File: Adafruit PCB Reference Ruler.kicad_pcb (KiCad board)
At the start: 2 copper layers, 101 x 25.4 mm, 63 parts

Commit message: Starting on schematic to PCB design
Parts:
- removed E$16, E$60, E$63: , Adafruit PCB Reference Ruler:0201
- removed E$23, E$61: , Adafruit PCB Reference Ruler:0402
- removed E$24, E$62: , Adafruit PCB Reference Ruler:0603
- removed E$25: , Adafruit PCB Reference Ruler:0805
- removed E$26: , Adafruit PCB Reference Ruler:1206
- removed E$27: , Adafruit PCB Reference Ruler:1210
- removed E$28: , Adafruit PCB Reference Ruler:2010
- removed E$58: , Adafruit PCB Reference Ruler:TQFP32-5MM
- added R1: R201, Resistors_SMD:R_0201, F.Cu at (85.9, 110.8)
- added R10: R1210, Resistors_SMD:R_1210, F.Cu at (95.6, 111.2)
- added R11: R2010, Resistors_SMD:R_2010, F.Cu at (98.9, 112.3)
- added R2: R201, Resistors_SMD:R_0201, F.Cu at (85.9, 112.1)
- added R3: R201, Resistors_SMD:R_0201, F.Cu at (85.9, 113.3)
- added R4: R402, Resistors_SMD:R_0402, F.Cu at (87.6, 112.9)
- added R5: R402, Resistors_SMD:R_0402, F.Cu at (87.7, 110.0)
- added R6: R603, Resistors_SMD:R_0603, F.Cu at (89.1, 112.8)
- added R7: R603, Resistors_SMD:R_0603, F.Cu at (89.1, 110.4)
- added R8: R805, Resistors_SMD:R_0805, F.Cu at (90.8, 110.7)
- added R9: R1206, Resistors_SMD:R_1206, F.Cu at (92.9, 111.3)
- added U1: 1.00, Adafruit PCB Reference Ruler:Pin_Header_Straight_1x01_Pitch1.00mm, F.Cu at (55.9, 115.2)
- added U2: 1.27, Adafruit PCB Reference Ruler:Pin_Header_Straight_1x01_Pitch1.27mm, F.Cu at (57.3, 115.1)
- added U3: 2.00, Adafruit PCB Reference Ruler:Pin_Header_Straight_1x01_Pitch2.00mm, F.Cu at (58.9, 115.0)
- added U4: 2.54, Adafruit PCB Reference Ruler:Pin_Header_Straight_1x01_Pitch2.54mm, F.Cu at (60.8, 114.8)
- E$17, E$18, E$19: footprint Adafruit PCB Reference Ruler:EDGE-INCHES-EIGTH -> Adafruit PCB Reference Ruler:EDGE-INCHES-TENTH
- E$20: footprint Adafruit PCB Reference Ruler:EDGE-INCHES-EIGTH2 -> Adafruit PCB Reference Ruler:EDGE-INCHES-TENTH
- moved E$55 21.7 mm to (136.4, 115.0)
- moved E$44 2.04 mm to (114.3, 100.8), turned to 90 degrees
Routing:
- net /Via: vias 0 -> 1
- added copper zone on F.Cu, net /Via
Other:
- board text added: "0201(0603) .05 0402(1005) .06 0603(1608) .10 0805(2012) .13"
- board text added: "1.00 1.27 2.00 2.54"
- board text added: "1/10 in"
- board text added: "1206(3216) .25"
- board text added: "1210(3225) .50"
- board text added: "2010(5025) .75"
- board text added: "Imperial(Metric) Watts"
- board text added: "Via"
- board text added: "mm"
- board text removed: "0201(0603) 0402(1005) 0603(1608) 0805(2012)"
- board text removed: "1/8"
- board text removed: "1206(3216)"
- board text removed: "1210(3225)"
- board text removed: "2010(5025)"
- board text removed: "Imperial (Metric)"
- board text removed: "QFP"

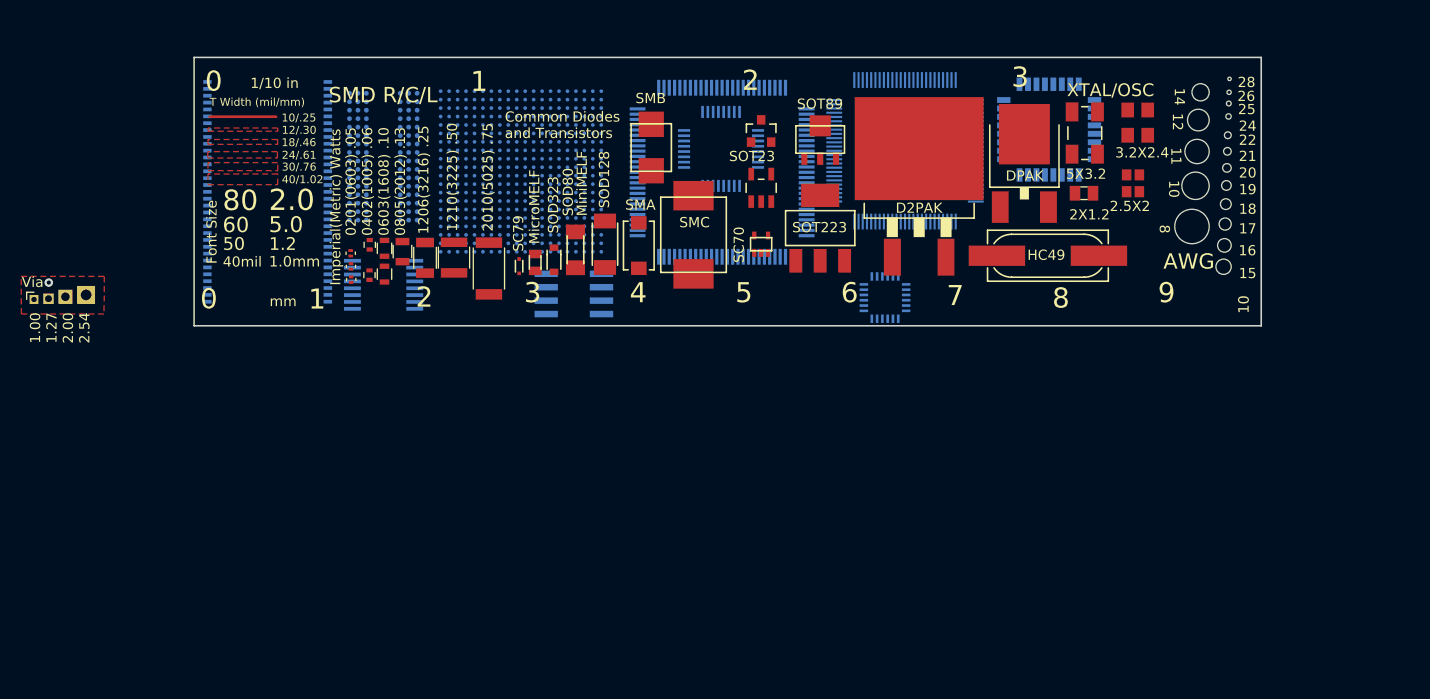
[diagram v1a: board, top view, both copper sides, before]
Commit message: Updated PCB to use KiCad standard parts (mostly)
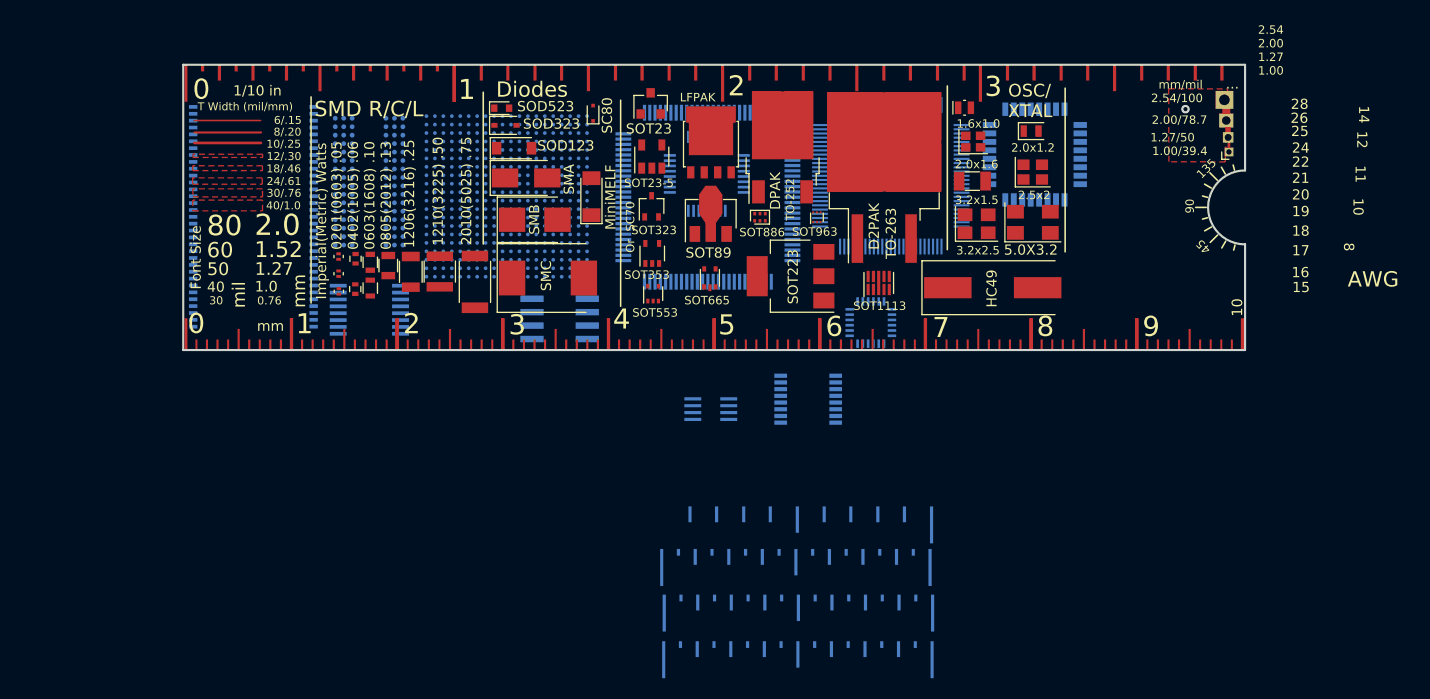
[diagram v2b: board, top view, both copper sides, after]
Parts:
- removed E$1, E$10, E$2, E$3, E$4, E$5, E$6, E$7, E$8, E$9: , Adafruit PCB Reference Ruler:EDGE-MILLIMETERS
- removed E$17, E$18, E$19, E$20: , Adafruit PCB Reference Ruler:EDGE-INCHES-TENTH
- removed E$29: , Adafruit PCB Reference Ruler:DPAK
- removed E$30: , Adafruit PCB Reference Ruler:D2PAK
- removed E$31: , Adafruit PCB Reference Ruler:SOT223
- removed E$32: , Adafruit PCB Reference Ruler:SOT89
- removed E$33: , Adafruit PCB Reference Ruler:SOT23-5
- removed E$34: , Adafruit PCB Reference Ruler:SOT23-3
- removed E$35: , Adafruit PCB Reference Ruler:SC70
- removed E$36: , Adafruit PCB Reference Ruler:CRYSTAL-SMD-5X3.2
- removed E$37: , Adafruit PCB Reference Ruler:CRYSTAL-SMD-3.2X2.5
- removed E$38: , Adafruit PCB Reference Ruler:CRYSTAL-SMD-2.5X2
- removed E$39: , Adafruit PCB Reference Ruler:HC49UP
- removed E$40: , Adafruit PCB Reference Ruler:XTAL-2X1.2
- removed E$41: , Adafruit PCB Reference Ruler:MICROMELF-R
- removed E$42: , Adafruit PCB Reference Ruler:SC79_INFINEON
- removed E$43: , Adafruit PCB Reference Ruler:SMA-DIODE
- removed E$44: , Adafruit PCB Reference Ruler:SMB-DIODE
- removed E$45: , Adafruit PCB Reference Ruler:SMC
- removed E$46: , Adafruit PCB Reference Ruler:ALL-HOLES2
- removed E$47: , Adafruit PCB Reference Ruler:SOD-128
- removed E$48: , Adafruit PCB Reference Ruler:SOD-323
- removed E$49: , Adafruit PCB Reference Ruler:SOD80C
- added D1: DSC80, Diodes_SMD:D_SC-80, F.Cu at (108.8, 97.6)
- added D2: DSOD123, Diodes_SMD:D_SOD-123, F.Cu at (101.3, 100.9)
- added D3: DSOD323, Diodes_SMD:D_SOD-323, F.Cu at (100.5, 98.7)
- added D4: DSOD523, Diodes_SMD:D_SOD-523, F.Cu at (100.1, 97.1)
- added D5: DSMA, Diodes_SMD:D_SMA, F.Cu at (102.5, 103.7)
- added D6: DSMB, Diodes_SMD:D_SMB, F.Cu at (103.3, 107.7)
- added D7: DSMC, Diodes_SMD:D_SMC, F.Cu at (104.5, 113.2)
- added D8: DminiMELF, Diodes_SMD:D_MiniMELF, F.Cu at (108.6, 105.5)
- added Q1: SOT23-3, TO_SOT_Packages_SMD:SOT-23, F.Cu at (114.2, 96.7)
- added Q10: SOT89, TO_SOT_Packages_SMD:SOT-89-3, F.Cu at (119.9, 107.5)
- added Q11: SOT886, TO_SOT_Packages_SMD:SOT-886, F.Cu at (124.6, 107.4)
- added Q12: SOT963, TO_SOT_Packages_SMD:SOT-963, F.Cu at (130.0, 107.4)
- added Q13: SSOP-16, Housings_SSOP:SSOP-16_3.9x4.9mm_Pitch0.635mm, B.Cu at (129.2, 124.7)
- added Q14: SSOP-8, Housings_SSOP:SSOP-8_2.95x2.8mm_Pitch0.65mm, B.Cu at (119.9, 125.6)
- added Q15: SOT1113, TO_SOT_Packages_SMD:SOT-1333-1, F.Cu at (135.8, 113.7)
- added Q16: SOT665, TO_SOT_Packages_SMD:SOT-665, F.Cu at (119.8, 113.2)
- added Q2: SOT23-5, TO_SOT_Packages_SMD:SOT-23-5, F.Cu at (114.3, 101.7)
- added Q3: SOT323, TO_SOT_Packages_SMD:SOT-323_SC-70, F.Cu at (114.3, 106.4)
- added Q4: SOT353, TO_SOT_Packages_SMD:SOT-353_SC-70-5, F.Cu at (114.4, 110.9)
- added Q5: SOT553, TO_SOT_Packages_SMD:SOT-553, F.Cu at (114.5, 114.7)
- added Q6: DPAK, TO_SOT_Packages_SMD:TO-252-2, F.Cu at (126.7, 100.8)
- added Q7: DP2AK, TO_SOT_Packages_SMD:TO-263-2, F.Cu at (136.3, 103.7)
- added Q8: LFPAK, TO_SOT_Packages_SMD:SOT-669_LFPAK, F.Cu at (120.0, 100.3)
- added Q9: SOT223, TO_SOT_Packages_SMD:SOT-223, F.Cu at (127.5, 113.0)
- added U10: 5mm, Adafruit PCB Reference Ruler:EDGE-MILLIMETERS, F.Cu at (120.2, 120.0)
- added U11: 6mm, Adafruit PCB Reference Ruler:EDGE-MILLIMETERS, F.Cu at (130.2, 120.0)
- added U12: 7mm, Adafruit PCB Reference Ruler:EDGE-MILLIMETERS, F.Cu at (140.2, 120.0)
- added U13: 8mm, Adafruit PCB Reference Ruler:EDGE-MILLIMETERS, F.Cu at (150.2, 120.0)
- added U14: 9mm, Adafruit PCB Reference Ruler:EDGE-MILLIMETERS, F.Cu at (160.2, 120.0)
- added U15: 3_10in, Adafruit PCB Reference Ruler:EDGE-INCHES-TENTH, B.Cu at (140.8, 134.8)
- added U16: 0_16in, Adafruit PCB Reference Ruler:EDGE-INCHES-SIXTEENTH, B.Cu at (140.7, 138.8)
- added U17: 1_16in, Adafruit PCB Reference Ruler:EDGE-INCHES-SIXTEENTH, B.Cu at (140.9, 143.1)
- added U18: 2_16in, Adafruit PCB Reference Ruler:EDGE-INCHES-SIXTEENTH, B.Cu at (140.9, 147.6)
- added U19: 3_16in, Adafruit PCB Reference Ruler:EDGE-INCHES-SIXTEENTH, F.Cu at (70.2, 93.0)
- added U20: 0_10in, Adafruit PCB Reference Ruler:EDGE-INCHES-TENTH, F.Cu at (95.7, 93.0)
- added U21: 1_10in, Adafruit PCB Reference Ruler:EDGE-INCHES-TENTH, F.Cu at (121.0, 93.0)
- added U22: 2_10in, Adafruit PCB Reference Ruler:EDGE-INCHES-TENTH, F.Cu at (145.4, 93.0)
- added U5: 0mm, Adafruit PCB Reference Ruler:EDGE-MILLIMETERS, F.Cu at (70.2, 120.0)
- added U6: 1mm, Adafruit PCB Reference Ruler:EDGE-MILLIMETERS, F.Cu at (80.2, 120.0)
- added U7: 2mm, Adafruit PCB Reference Ruler:EDGE-MILLIMETERS, F.Cu at (90.2, 120.0)
- added U8: 3mm, Adafruit PCB Reference Ruler:EDGE-MILLIMETERS, F.Cu at (100.2, 120.0)
- added U9: 4mm, Adafruit PCB Reference Ruler:EDGE-MILLIMETERS, F.Cu at (110.2, 120.0)
- added XT1: HC49, Crystals:Crystal_SMD_HC49-SD, F.Cu at (146.6, 114.1)
- added XT2: 1.6x1.0, Crystals:Crystal_SMD_MicroCrystal_CM9V-T1A-2pin_1.6x1.0mm, F.Cu at (143.9, 97.1)
- added XT3: 2.0x1.2, Crystals:Crystal_SMD_2012-2pin_2.0x1.2mm, F.Cu at (150.2, 99.3)
- added XT4: 2.0x1.6, Crystals:Crystal_SMD_2016-4pin_2.0x1.6mm, F.Cu at (144.8, 100.3)
- added XT5: 3.2x2.5, Crystals:Crystal_SMD_3225-4pin_3.2x2.5mm, F.Cu at (145.1, 108.0)
- added XT6: 5x3.2, Crystals:Crystal_SMD_5032-4pin_5.0x3.2mm, F.Cu at (150.4, 107.9)
- added XT7: 2.5x2, Crystals:Crystal_SMD_2520-4pin_2.5x2.0mm, F.Cu at (150.4, 103.2)
- added XT8: 3.2x1.5, Crystals:Crystal_SMD_3215-2pin_3.2x1.5mm, F.Cu at (144.7, 104.0)
- moved U1 114.0 mm to (169.0, 101.2), turned to 90 degrees
- moved U2 112.7 mm to (168.9, 99.9), turned to 90 degrees
- moved U3 111.1 mm to (168.7, 98.3), turned to 90 degrees
- moved U4 109.3 mm to (168.5, 96.3), turned to 90 degrees
- moved E$66 2.72 mm to (76.6, 107.4)
- moved E$69 2.72 mm to (150.6, 101.5)
- moved E$71 2.72 mm to (87.6, 104.1)
- moved E$56 2.72 mm to (87.7, 116.1)
- moved E$57 2.72 mm to (105.6, 117.1)
- moved E$65 2.72 mm to (119.7, 105.5)
- moved E$67 2.72 mm to (100.6, 105.5)
- moved E$70 2.72 mm to (119.6, 103.3)
- moved E$68 2.72 mm to (137.0, 103.5)
- moved E$55 2.72 mm to (135.1, 117.4)
- moved R7 1.89 mm to (87.7, 111.7)
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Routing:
- net (no net): track 6.30 -> 18.9 mm
- net /Via: track 0.00 -> 5.36 mm
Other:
- board size 101 x 25.4 mm -> 100.5 x 27 mm
- board text added: "..."
- board text added: "0.76"
- board text added: "1.0"
- board text added: "1.00/39.4"
- board text added: "1.27"
- board text added: "1.27/50"
- board text added: "1.52"
- board text added: "1.6x1.0"
- board text added: "135"
- board text added: "2.00/78.7"
- board text added: "2.0x1.2"
- board text added: "2.0x1.6"
- board text added: "2.54 2.00 1.27 1.00"
- board text added: "2.54/100"
- board text added: "2.5x2"
- board text added: "3.2x1.5"
- board text added: "3.2x2.5"
- board text added: "30"
- board text added: "40"
- board text added: "40/1.0"
- board text added: "45"
- board text added: "5.0X3.2"
- board text added: "6/.15"
- board text added: "8/.20"
- board text added: "90"
- board text added: "Diodes"
- board text added: "LFPAK"
- board text added: "OSC/ XTAL"
- board text added: "Or SC70"
- board text added: "SC80"
- board text added: "SOD123"
- board text added: "SOD523"
- board text added: "SOT1113"
- board text added: "SOT23-5"
- board text added: "SOT323"
- board text added: "SOT353"
- board text added: "SOT553"
- board text added: "SOT665"
- board text added: "SOT886"
- board text added: "SOT963"
- board text added: "SSOP -16"
- board text added: "SSOP-8"
- board text added: "TO-252"
- board text added: "TO-263"
- board text added: "mil"
- board text added: "mm/mil"
- board text removed: "1.00 1.27 2.00 2.54"
- board text removed: "1.0mm"
- board text removed: "1.2"
- board text removed: "2.5X2"
- board text removed: "2X1.2"
- board text removed: "3.2X2.4"
- board text removed: "40/1.02"
- board text removed: "40mil"
- board text removed: "5.0"
- board text removed: "5X3.2"
- board text removed: "Common Diodes and Transistors"
- board text removed: "MicroMELF"
- board text removed: "SC70"
- board text removed: "SC79"
- board text removed: "SOD128"
- board text removed: "SOD80"
- board text removed: "Via"
- board text removed: "XTAL/OSC"
